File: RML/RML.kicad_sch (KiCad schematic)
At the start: 18 parts, among them U1 74AHC1G02, U102 641964-1, U103 641964-1, U104 LM555xM, U2 LM7805_TO220, U3 SFH617A-1

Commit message: add useful commit messages they say
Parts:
- removed R1: 35k, symbol Device:R_US
- added R3, R4, R5, R6, R7, R8: 4.7k, Resistor_SMD:R_2512_6332Metric_Pad1.40x3.35mm_HandSolder, symbol Device:R_US
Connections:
- net 352.8V: now reaches U103.1
- net 352.8V: now also R3.2
- net 12.5 mA: now reaches U3.1
- new net: R6.1, R7.2
- new net: R5.1, R6.2
- new net: R4.1, R5.2
- new net: R3.1, R4.2
- new net: R7.1, R8.2
- new net 12.5mA: R8.1
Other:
- note added: "Power Dissapation/ Current limiter"
- note removed: "10mA @ 3.5W"

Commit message: RML footprints
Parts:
- C1: footprint (none) -> Capacitor_SMD:C_0402_1005Metric; JLC# (none) -> C107013
- C101: footprint (none) -> Capacitor_SMD:C_0201_0603Metric
- C105: value C -> 22u; JLC# (none) -> C105226
- C2: footprint (none) -> Capacitor_SMD:C_0402_1005Metric; JLC# (none) -> C1524
- Q1: renamed from Q?; footprint (none) -> Package_TO_SOT_THT:TO-220-3_Vertical; JLC# (none) -> C2562
- R102: footprint (none) -> Capacitor_SMD:C_0402_1005Metric; JLC# (none) -> C102759
- R105: value R_US -> 15k; footprint (none) -> Capacitor_SMD:C_0402_1005Metric; JLC# (none) -> C25756
- R106: footprint (none) -> Capacitor_SMD:C_0402_1005Metric
- R2: footprint (none) -> Capacitor_SMD:C_0402_1005Metric; JLC# (none) -> C102750
- R3, R4, R5, R6, R7, R8: JLC# (none) -> C163339
- U1: footprint (none) -> Package_TO_SOT_SMD:SOT-23-5; JLC# (none) -> C7463
- U104: JLC# (none) -> C90760
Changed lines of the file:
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@@
+			"AAAAAAAAAAAAAAAAAAAAAAAAAAAAAAAAAAAAAAAAAAAAAAAAAAAAAAAAAAAAAAAAAAAAAAAAAAAA"
+			"AAAAAAAAAAAAAAAAAAAAAAAAAAAAAAAAAAAAAAAAAAAAAAAAAAAAAAAAAAAAAAAAAAAAAAAAAAAA"
+			"AAAAAAAAAAAAAAAAAAAAAAAAAAAAAAAAAAAAAAAAAAAAAAAAAAAAAAAAAAAAAAAAAAAAAAAAAAAA"
+			"AAAAAAAAAAAAAAAAAAAAAAAAAAAAAAAAAAAAAAAAAAAAAAAAAAAAAAAAAAAAAAAAAAAAAAAAAAAA"
+			"AAAAAAAAAAAAAAAAAAAAAAAAAAAAAAAAAAAAAAAAAAAAAAAAAAAAAAAAAAAAAAAAAAAAAAAAAAAA"
+			"AAAAAAAAAAAAAAAAAAAAAAAAAAAAAAAAAAAAAAAAAAAAAAAAAAAAAAAAAAAAAAAAAAAAAAAAAAAA"
+			"AAAAAAAAAAAAAAAAAAAAAAAAAAAAAAAAAAAAAAAAAAAAAAAAAAAAAAAAAAAAAAAAAAAAAAAAAAAA"
+			"AAAAAAAAAAAAAAAAAAAAAAAAAAAAAAAAAAAAAAAAAAAAAAAAAAAAAAAAAAAAAAAAAAAAAAAAAAAA"
+			"AAAAAAAAAAAAAAAAAAAAAAAAAAAAAAAAAAAAAAAAAAAAAAAAAAAAAAAAAAAAAAAAAAAAAAAAAAAA"
+			"AAAAAAAAAAAAAAAAAAAAAAAAAAAAAAAAAAAAAAAAAAAAAAAAAAAAAAAAAAAAAAAAAAAAAAAAAAAA"
+			"AAAAAAAAAAAAAAAAAAAAAAAAAAAAAAAAAAAAAAAAAAAAAAAAAAAAAAAAAAAAAAAAAAAAAAAAAAAA"
+			"AAAAAAAAAAAAAAAAAAAAAAAAAAAAAAAAAAAAAAAAAAAAAAAAAAAAAAAAAAAAAAAAAAAAAAAAAAAA"
+			"AAAAAAAAAAAAAAAAAAAAAAAAAAAAAAAAAAAAAAAAAAAAAAAAAAAAAAAAAAAAAAAAAAAAAAAAAAAA"
+			"AAAAAAAAAAAAAAAAAAAAAAAAAAAAAAAAAAAAAAAAAAAAAAAAAAAAAAAAAAAAAAAAAAAAAAAAAAAA"
+			"AAAAAAAAAAAAAAAAAAAAAAAAAAAAAAAAAAAAAAAAAAAAAAAAAAAAAAAAAAAAAAAAAAAAAAAAAAAA"
+			"AAAAAAAAAAAAAAAAAAAAAAAAAAAAAAAAAAAAAAAAAAAAAAAAAAAAAAAAAAAAAAAAAAAAAAAAAAAA"
+			"AAAAAAAAAAAAAAAAAAAAAAAAAAAAAAAAAAAAAAAAAAAAAAAAAAAAAAAAAAAAAAAAAAAAAAAAAAAA"
+			"AAAAAAAAAAAAAAAAAAAAAAAAAAAAAAAAAAAAAAAAAAAAAAAAAAAAAAAAAAAAAAAAAAAAAAAAAAAA"
 			"AAAAAAAAAAAAAAAAAAAAAAAAAAAAAAAAAAAAAAAAAAAAAAAAAAAAAAAAAAAAAAAAAAAAAAAAAAAA"
 			"AAAAAAAAAAAAAAAAAAAAAAAAAAAAAAAAAAAAAAAAAAAAAAAAAAAAAAAAAAAAAAAAAAAAAAAAAAAA"
@@
 			)
 		)
-		(property "Footprint" ""
+		(property "Footprint" "Capacitor_SMD:C_0402_1005Metric"
 			(at 177.8 64.4652 0)
 			(effects
@@
 			)
 		)
-		(property "Datasheet" "~"
+		(property "Datasheet" "https://jlcpcb.com/api/file/downloadByFileSystemAccessId/8588894393365368832"
 			(at 181.61 63.5 0)
 			(effects
@@
 			)
 		)
+		(property "JLC#" "C1524"
+			(at 181.61 63.5 90)
+			(effects
+				(font
+					(size 1.27 1.27)
+				)
+				(hide yes)
+			)
+		)
 		(pin "1"
 		)
@@
 			)
 		)
+		(property "JLC#" "C163339"
+			(at 64.77 26.67 90)
+			(effects
+				(font
+					(size 1.27 1.27)
+				)
+				(hide yes)
+			)
+		)
 		(pin "1"
 		)
@@
 			)
 		)
-		(property "Value" "R_US"
+		(property "Value" "15k"
 			(at 80.01 153.67 90)
 			(effects
@@
 			)
 		)
-		(property "Footprint" ""
+		(property "Footprint" "Capacitor_SMD:C_0402_1005Metric"
 			(at 73.914 153.416 90)
 			(effects
@@
 			)
 		)
-		(property "Datasheet" "~"
+		(property "Datasheet" "https://jlcpcb.com/api/file/downloadByFileSystemAccessId/8579705971410853888"
 			(at 74.93 153.67 0)
 			(effects
@@
 			)
 		)
-		(property "JLC#" ""
+		(property "JLC#" "C25756"
 			(at 74.93 153.67 0)
 			(effects
@@
 			)
 		)
-		(property "Footprint" ""
+		(property "Footprint" "Capacitor_SMD:C_0402_1005Metric"
 			(at 219.964 89.916 90)
 			(effects
@@
 			)
 		)
-		(property "Datasheet" "~"
+		(property "Datasheet" "https://jlcpcb.com/api/file/downloadByFileSystemAccessId/8588898236594081792"
 			(at 220.98 90.17 0)
 			(effects
@@
 			)
 		)
+		(property "JLC#" "C102750"
+			(at 220.98 90.17 0)
+			(effects
+				(font
+					(size 1.27 1.27)
+				)
+				(hide yes)
+			)
+		)
 		(pin "1"
 		)
@@
 			)
 		)
+		(property "JLC#" "C163339"
+			(at 44.45 26.67 90)
+			(effects
+				(font
+					(size 1.27 1.27)
+				)
+				(hide yes)
+			)
+		)
 		(pin "1"
 		)
@@
 			)
 		)
-		(property "Footprint" ""
+		(property "Footprint" "Capacitor_SMD:C_0402_1005Metric"
 			(at 154.686 73.914 90)
 			(effects
@@
 			)
 		)
-		(property "Datasheet" "~"
+		(property "Datasheet" "https://jlcpcb.com/api/file/downloadByFileSystemAccessId/8588898237633323008"
 			(at 153.67 73.66 0)
 			(effects
@@
 			)
 		)
+		(property "JLC#" "C102759"
+			(at 153.67 73.66 0)
+			(effects
+				(font
+					(size 1.27 1.27)
+				)
+				(hide yes)
+			)
+		)
 		(pin "1"
 		)
@@
 		(dnp no)
 		(fields_autoplaced yes)
-		(property "Reference" "Q?"
+		(property "Reference" "Q1"
 			(at 245.11 83.8199 0)
 			(effects
@@
 			)
 		)
-		(property "Footprint" ""
+		(property "Footprint" "Package_TO_SOT_THT:TO-220-3_Vertical"
 			(at 243.84 82.55 0)
 			(effects
@@
 			)
 		)
-		(property "Datasheet" "https://ngspice.sourceforge.io/docs/ngspice-html-manual/manual.xhtml#cha_MOSFETs"
+		(property "Datasheet" "https://jlcpcb.com/api/file/downloadByFileSystemAccessId/8588896295771639808"
 			(at 238.76 97.79 0)
 			(effects
@@
 			)
 		)
+		(property "JLC#" "C2562"
+			(at 238.76 85.09 0)
+			(effects
+				(font
+					(size 1.27 1.27)
+				)
+				(hide yes)
+			)
+		)
 		(pin "3"
 		)
@@
 			(project ""
 				(path "/3ca2658d-b0d3-478f-88c8-e8564dea016d"
-					(reference "Q?")
+					(reference "Q1")
 					(unit 1)
 				)
@@
 			)
 		)
+		(property "JLC#" "C163339"
+			(at 85.09 26.67 90)
+			(effects
+				(font
+					(size 1.27 1.27)
+				)
+				(hide yes)
+			)
+		)
 		(pin "1"
 		)
@@
 			)
 		)
+		(property "JLC#" "C163339"
+			(at 34.29 26.67 90)
+			(effects
+				(font
+					(size 1.27 1.27)
+				)
+				(hide yes)
+			)
+		)
 		(pin "1"
 		)
@@
 			)
 		)
-		(property "Footprint" ""
+		(property "Footprint" "Capacitor_SMD:C_0201_0603Metric"
 			(at 24.13 151.13 0)
 			(effects
@@
 			)
 		)
-		(property "Footprint" ""
+		(property "Footprint" "Package_TO_SOT_SMD:SOT-23-5"
 			(at 189.23 85.09 0)
 			(effects
@@
 			)
 		)
-		(property "Datasheet" "http://www.ti.com/lit/sg/scyt129e/scyt129e.pdf"
+		(property "Datasheet" "https://www.ti.com/cn/lit/ds/symlink/sn74ahc1g02.pdf?ts=1743093850620&ref_url=https%253A%252F%252Fpro.easyeda.com%252F"
 			(at 189.23 85.09 0)
 			(effects
@@
 			)
 		)
+		(property "JLC#" "C7463"
+			(at 189.23 85.09 0)
+			(effects
+				(font
+					(size 1.27 1.27)
+				)
+				(hide yes)
+			)
+		)
 		(pin "3"
 		)
@@
 			)
 		)
+		(property "JLC#" "C163339 "
+			(at 74.93 26.67 90)
+			(effects
+				(font
+					(size 1.27 1.27)
+				)
+				(hide yes)
+			)
+		)
 		(pin "1"
 		)
@@
 			)
 		)
-		(property "Footprint" ""
+		(property "Footprint" "Capacitor_SMD:C_0402_1005Metric"
 			(at 160.9852 60.96 0)
 			(effects
@@
 			)
 		)
-		(property "Datasheet" "~"
+		(property "Datasheet" "https://jlcpcb.com/api/file/downloadByFileSystemAccessId/8588898744154116096"
 			(at 160.02 57.15 0)
 			(effects
@@
 			)
 		)
+		(property "JLC#" "C107013 "
+			(at 160.02 57.15 0)
+			(effects
+				(font
+					(size 1.27 1.27)
+				)
+				(hide yes)
+			)
+		)
 		(pin "2"
 		)
@@
 			)
 		)
-		(property "Value" "C"
+		(property "Value" "22u"
 			(at 88.9 184.1499 0)
 			(effects
@@
 			)
 		)
-		(property "Datasheet" "~"
+		(property "Datasheet" "https://jlcpcb.com/api/file/downloadByFileSystemAccessId/8589952084973027328"
 			(at 85.09 182.88 0)
 			(effects
@@
 			)
 		)
-		(property "JLC#" ""
+		(property "JLC#" "C105226 "
 			(at 85.09 182.88 0)
 			(effects
@@
 			)
 		)
-		(property "JLC#" ""
+		(property "JLC#" "C90760"
 			(at 60.96 166.37 0)
 			(effects
@@
 			)
 		)
-		(property "Footprint" ""
+		(property "Footprint" "Capacitor_SMD:C_0402_1005Metric"
 			(at 84.074 167.386 90)
 			(effects
@@
 			(effects
 				(font
+					(size 1.27 1.27)
+				)
+				(hide yes)
+			)
+		)
+		(property "JLC#" "C163339"
+			(at 54.61 26.67 90)
+			(effects
+				(font

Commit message: Broken pcb
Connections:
- net 12.5mA is gone; now on net 12.5 mA: R8.1
- net +5V: now reaches C2.1, U1.5 (VCC), U2.3 (VO)
- net +5V: now also C101.1, C102.1, R106.2, U104.4 (R), U104.8 (VCC)
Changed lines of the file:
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@@
+			"AAAAAAAAAAAAAAAAAAAAAAAAAAAAAAAAAAAAAAAAAAAAAAAAAAAAAAAAAAAAAAAAAAAAAAAAAAAA"
+			"AAAAAAAAAAAAAAAAAAAAAAAAAAAAAAAAAAAAAAAAAAAAAAAAAAAAAAAAAAAAAAAAAAAAAAAAAAAA"
+			"AAAAAAAAAAAAAAAAAAAAAAAAAAAAAAAAAAAAAAAAAAAAAAAAAAAAAAAAAAAAAAAAAAAAAAAAAAAA"
+			"AAAAAAAAAAAAAAAAAAAAAAAAAAAAAAAAAAAAAAAAAAAAAAAAAAAAAAAAAAAAAAAAAAAAAAAAAAAA"
+			"AAAAAAAAAAAAAAAAAAAAAAAAAAAAAAAAAAAAAAAAAAAAAAAAAAAAAAAAAAAAAAAAAAAAAAAAAAAA"
+			"AAAAAAAAAAAAAAAAAAAAAAAAAAAAAAAAAAAAAAAAAAAAAAAAAAAAAAAAAAAAAAAAAAAAAAAAAAAA"
+			"AAAAAAAAAAAAAAAAAAAAAAAAAAAAAAAAAAAAAAAAAAAAAAAAAAAAAAAAAAAAAAAAAAAAAAAAAAAA"
+			"AAAAAAAAAAAAAAAAAAAAAAAAAAAAAAAAAAAAAAAAAAAAAAAAAAAAAAAAAAAAAAAAAAAAAAAAAAAA"
+			"AAAAAAAAAAAAAAAAAAAAAAAAAAAAAAAAAAAAAAAAAAAAAAAAAAAAAAAAAAAAAAAAAAAAAAAAAAAA"
+			"AAAAAAAAAAAAAAAAAAAAAAAAAAAAAAAAAAAAAAAAAAAAAAAAAAAAAAAAAAAAAAAAAAAAAAAAAAAA"
+			"AAAAAAAAAAAAAAAAAAAAAAAAAAAAAAAAAAAAAAAAAAAAAAAAAAAAAAAAAAAAAAAAAAAAAAAAAAAA"
+			"AAAAAAAAAAAAAAAAAAAAAAAAAAAAAAAAAAAAAAAAAAAAAAAAAAAAAAAAAAAAAAAAAAAAAAAAAAAA"
+			"AAAAAAAAAAAAAAAAAAAAAAAAAAAAAAAAAAAAAAAAAAAAAAAAAAAAAAAAAAAAAAAAAAAAAAAAAAAA"
+			"AAAAAAAAAAAAAAAAAAAAAAAAAAAAAAAAAAAAAAAAAAAAAAAAAAAAAAAAAAAAAAAAAAAAAAAAAAAA"
+			"AAAAAAAAAAAAAAAAAAAAAAAAAAAAAAAAAAAAAAAAAAAAAAAAAAAAAAAAAAAAAAAAAAAAAAAAAAAA"
+			"AAAAAAAAAAAAAAAAAAAAAAAAAAAAAAAAAAAAAAAAAAAAAAAAAAAAAAAAAAAAAAAAAAAAAAAAAAAA"
+			"AAAAAAAAAAAAAAAAAAAAAAAAAAAAAAAAAAAAAAAAAAAAAAAAAAAAAAAAAAAAAAAAAAAAAAAAAAAA"
+			"AAAAAAAAAAAAAAAAAAAAAAAAAAAAAAAAAAAAAAAAAAAAAAAAAAAAAAAAAAAAAAAAAAAAAAAAAAAA"
 			"AAAAAAAAAAAAAAAAAAAAAAAAAAAAAAAAAAAAAAAAAAAAAAAAAAAAAAAAAAAAAAAAAAAAAAAAAAAA"
 			"AAAAAAAAAAAAAAAAAAAAAAAAAAAAAAAAAAAAAAAAAAAAAAAAAAAAAAAAAAAAAAAAAAAAAAAAAAAA"
@@
 		)
 	)
-	(global_label "12.5mA"
+	(global_label "12.5 mA"
 		(shape input)
 		(at 92.71 26.67 0)
@@
 		)
 		(property "Intersheetrefs" "${INTERSHEET_REFS}"
-			(at 102.7104 26.67 0)
+			(at 103.678 26.67 0)
 			(effects
 				(font
@@
 	)
 	(symbol
+		(lib_id "power:+5V")
+		(at 60.96 139.7 0)
+		(unit 1)
+		(exclude_from_sim no)
+		(in_bom yes)
+		(on_board yes)
+		(dnp no)
+		(fields_autoplaced yes)
+		(property "Reference" "#PWR04"
+			(at 60.96 143.51 0)
+			(effects
+				(font
+					(size 1.27 1.27)
+				)
+				(hide yes)
+			)
+		)
+		(property "Value" "+5V"
+			(at 60.96 134.62 0)
+			(effects
+				(font
+					(size 1.27 1.27)
+				)
+			)
+		)
+		(property "Footprint" ""
+			(at 60.96 139.7 0)
+			(effects
+				(font
+					(size 1.27 1.27)
+				)
+				(hide yes)
+			)
+		)
+		(property "Datasheet" ""
+			(at 60.96 139.7 0)
+			(effects
+				(font
+					(size 1.27 1.27)
+				)
+				(hide yes)
+			)
+		)
+		(property "Description" "Power symbol creates a global label with name \"+5V\""
+			(at 60.96 139.7 0)
+			(effects
+				(font
+					(size 1.27 1.27)
+				)
+				(hide yes)
+			)
+		)
+		(pin "1"
+		)
+		(instances
+			(project ""
+				(path "/3ca2658d-b0d3-478f-88c8-e8564dea016d"
+					(reference "#PWR04")
+					(unit 1)
+				)
+			)
+		)
+	)
+	(symbol
 		(lib_id "Device:R_US")
 		(at 74.93 153.67 180)
@@
 					(unit 1)
 				)
+			)
+		)
+	)
+	(symbol
+		(lib_id "power:+5V")
+		(at 189.23 63.5 270)
+		(unit 1)
+		(exclude_from_sim no)
+		(in_bom yes)
+		(on_board yes)
+		(dnp no)
+		(fields_autoplaced yes)
+		(property "Reference" "#PWR05"
+			(at 185.42 63.5 0)
+			(effects
+				(font
+					(size 1.27 1.27)
+				)
+				(hide yes)
+			)
+		)
+		(property "Value" "+5V"
+			(at 193.04 63.4999 90)
+			(effects
+				(font
+					(size 1.27 1.27)
+				)
+				(justify left)
+			)
+		)
+		(property "Footprint" ""
+			(at 189.23 63.5 0)
+			(effects
+				(font
+					(size 1.27 1.27)
+				)
+				(hide yes)
+			)
+		)
+		(property "Datasheet" ""
+			(at 189.23 63.5 0)
+			(effects
+				(font
+					(size 1.27 1.27)
+				)
+				(hide yes)
+			)
+		)
+		(property "Description" "Power symbol creates a global label with name \"+5V\""
+			(at 189.23 63.5 0)
+			(effects
+				(font
+					(size 1.27 1.27)
+				)
+				(hide yes)
+			)
+		)
+		(pin "1"
+		)
+		(instances
+			(project ""
+				(path "/3ca2658d-b0d3-478f-88c8-e8564dea016d"
+					(reference "#PWR05")
+					(unit 1)
+				)

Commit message: Changes to RML and TSSI
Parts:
- removed Q1: NMOS, Package_TO_SOT_THT:TO-220-3_Vertical, symbol Simulation_SPICE:NMOS
- added Q101, Q102: Q_NMOS_Depletion_GDS, Package_TO_SOT_THT:TO-220-3_Vertical, symbol Transistor_FET_Other:Q_NMOS_Depletion_GDS
- added U105: 641964-1, 641964-1_TYC, symbol CONNECTOR:641964-1
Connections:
- net +12V: now also U105.1; no longer R102.1
- net +5V: now also R102.1
- net GND: now also Q101.3 (S), Q102.3 (S), U105.2; no longer U102.2
- net DRIVE: now reaches R2.2, U1.4
- net DRIVE: now also Q101.1 (G), Q102.1 (G)
- net at U102.1: now also Q101.2 (D)
- new net: Q102.2 (D), U102.2
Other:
- note added: "+ Side of light connncts directly to GLV - Side of light connects to RML board"
- note added: "POWER MOSFETS"
- note removed: "(12.8 V - 0.243 A) * 2"
- note removed: "POWER MOSFET"
- moved on the sheet: C1, C101, C102, C103, C105, C2, R105, R106, R2, R3, R4, R5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

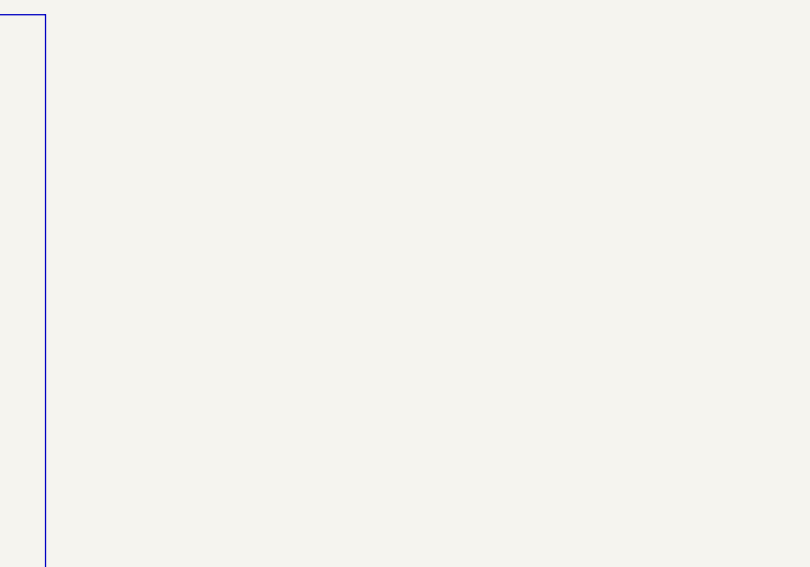
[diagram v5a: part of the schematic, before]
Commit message: Added changes to RML and re-routed to fit on 1 layer
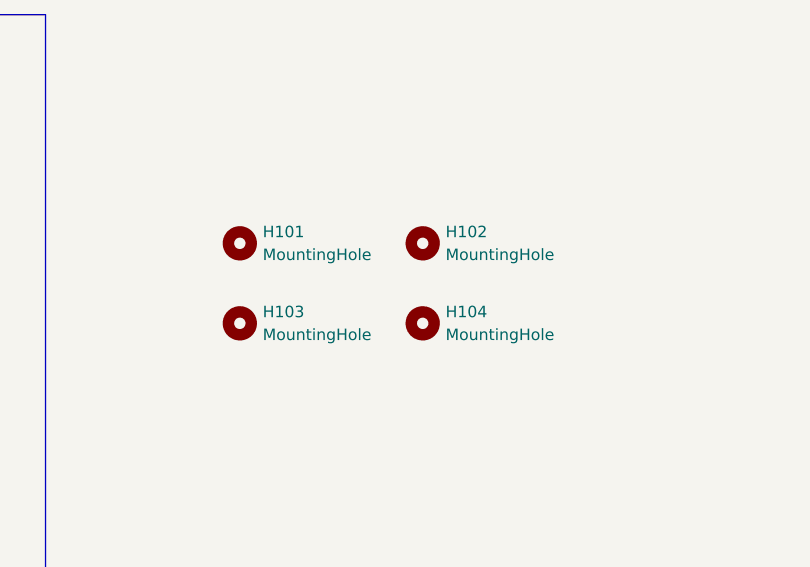
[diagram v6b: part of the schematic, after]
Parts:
- added H101, H102, H103, H104: MountingHole, MountingHole:MountingHole_3.2mm_M3, symbol Mechanical:MountingHole

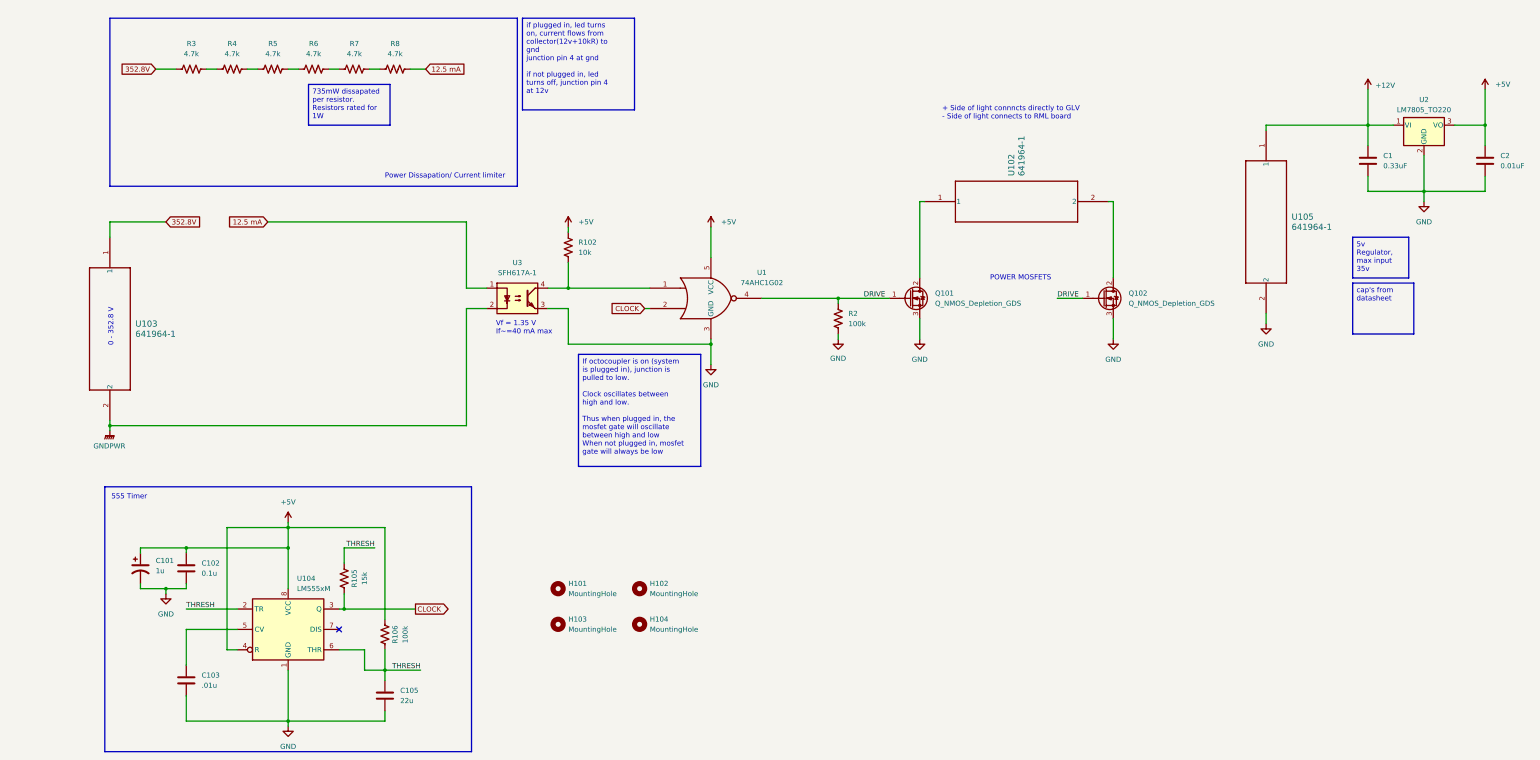
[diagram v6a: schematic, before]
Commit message: Updated RML BOM
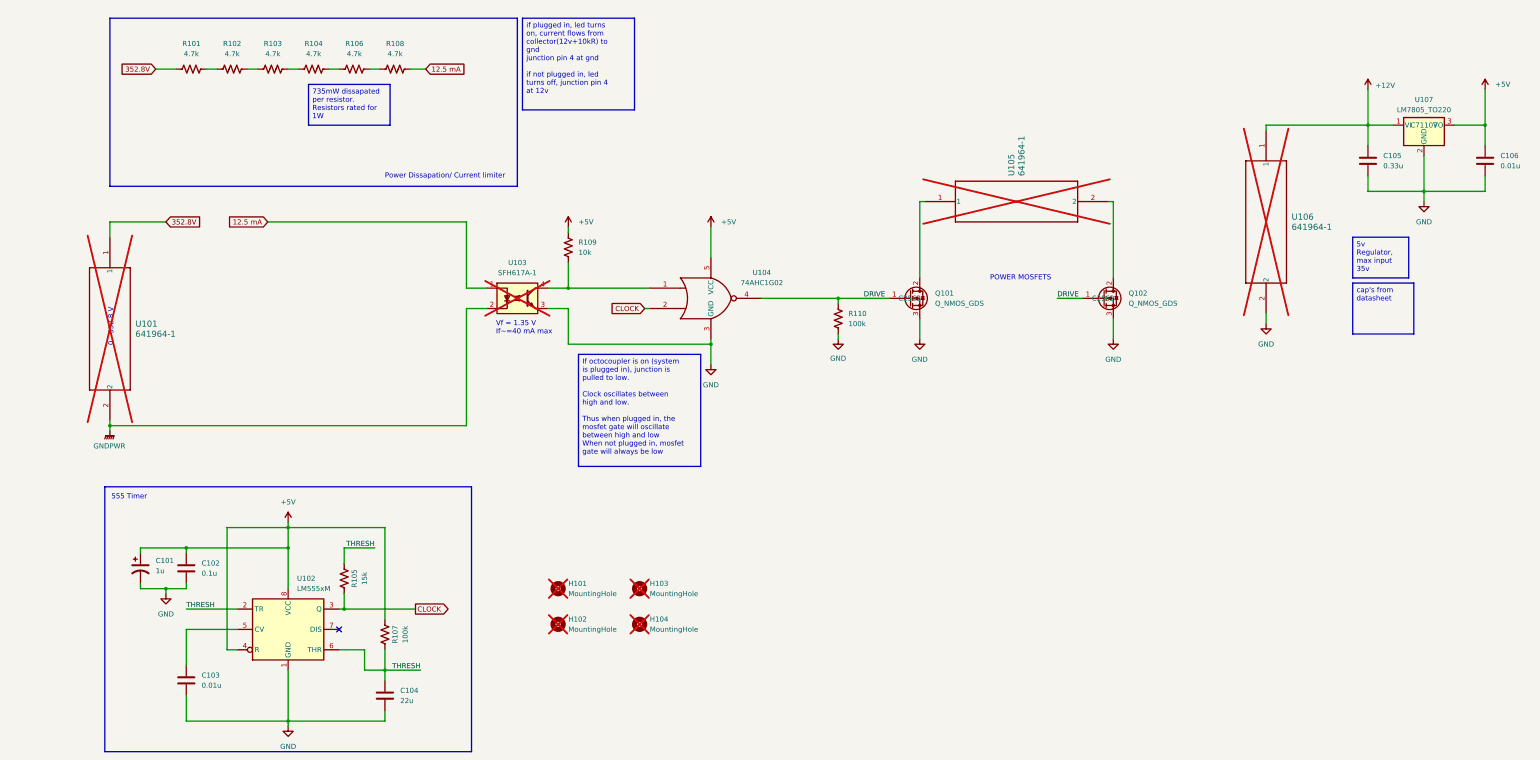
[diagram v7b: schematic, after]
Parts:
- removed Q101, Q102: Q_NMOS_Depletion_GDS, Package_TO_SOT_THT:TO-220-3_Vertical, symbol Transistor_FET_Other:Q_NMOS_Depletion_GDS
- added Q101, Q102: Q_NMOS_GDS, Package_TO_SOT_THT:TO-220-3_Vertical, symbol Transistor_FET:Q_NMOS_GDS
- C103: value .01u -> 0.01u
- C105: renamed from C1; value 0.33uF -> 0.33u
- C106: renamed from C2; value 0.01uF -> 0.01u; JLC# C1524 -> C15195
- H101, H104: now not fitted
- H102: renamed from H103; now not fitted
- H103: renamed from H102; now not fitted
- R107: renamed from R106; JLC# C60491 -> C102750
- U101: renamed from U103; now not fitted
- U103: renamed from U3; now not fitted
- U105: renamed from U102; now not fitted
- U106: renamed from U105; now not fitted
- U107: renamed from U2; JLC# (none) -> C71107
- renumbered C105 to C104, R3 to R101, R4 to R102, R5 to R103, R6 to R104, R7 to R106, R8 to R108, R102 to R109, R2 to R110, U104 to U102, U1 to U104
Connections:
- net DRIVE: now also Q101.1 (G), Q102.1 (G)
- net GND: now also Q101.3 (S), Q102.3 (S)
- net at U105.1: now also Q101.2 (D)
- net at U105.2: now also Q102.2 (D)
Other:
- note removed: "+ Side of light connncts directly to GLV - Side of light connects to RML board"
